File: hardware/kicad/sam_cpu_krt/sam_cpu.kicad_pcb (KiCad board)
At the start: 4 copper layers, 142 x 236.8 mm, 459 parts, among them J1 J1 SWITCH COLUMNS, J10 J10 SPEAKERS, J11 J11 POWER, J12 J12 SWITCH ROWS, J13 J13 DEDICATED, J17 EXT 5V, J18 J18 GI DIMMER, J19 USB-C (to Pi), J2 J2 DEDICATED, J20 SWD, J21 Raspberry Pi 40-pin, J22 J22 STEREO, J23 EXT 12V, J24 J24 SUBWOOFER, J27 J27 RS485 IN, J28 J28 I2S IN, J29 J29 RS485 OUT, J3 J3 DEDICATED, J30 J30 LINE IN, J6 J6 SWITCH ROWS, J9 J9 IO BUS, Q1 AO3401A, Q11 MMBT3904, Q12 MMBT3904, Q13 MMBT3904, Q14 MMBT3904, Q15 MMBT3904, Q16 MMBT3904, Q17 MMBT3904, Q18 MMBT3904, Q2 AO3401A, Q3 2N7002, Q4 2N7002, SW1 RESET, SW2 BOOTSEL, SW3 DIP x8, U1 LTC4412, U10 LM339, U11 LM339, U14 74HC165, U15 74HC165, U16 74HC165, U17 74HC165, U18 74HC165, U19 74HC165, U2 LTC4412, U20 74HC595, U22 PCM5102A, U23 TDA7297, U24 TDA7297, U25 DS3231MZ, U26 OPA1678, U3 NCP1117-3.3, U30 74HC165, U31 74HC595, U32 ADM2682E, U4 RP2354B, U5 TPS3808G33, U6 SN74LVC8T245, U7 74AHCT541, U8 LM339, U9 LM339, Y1 12MHz

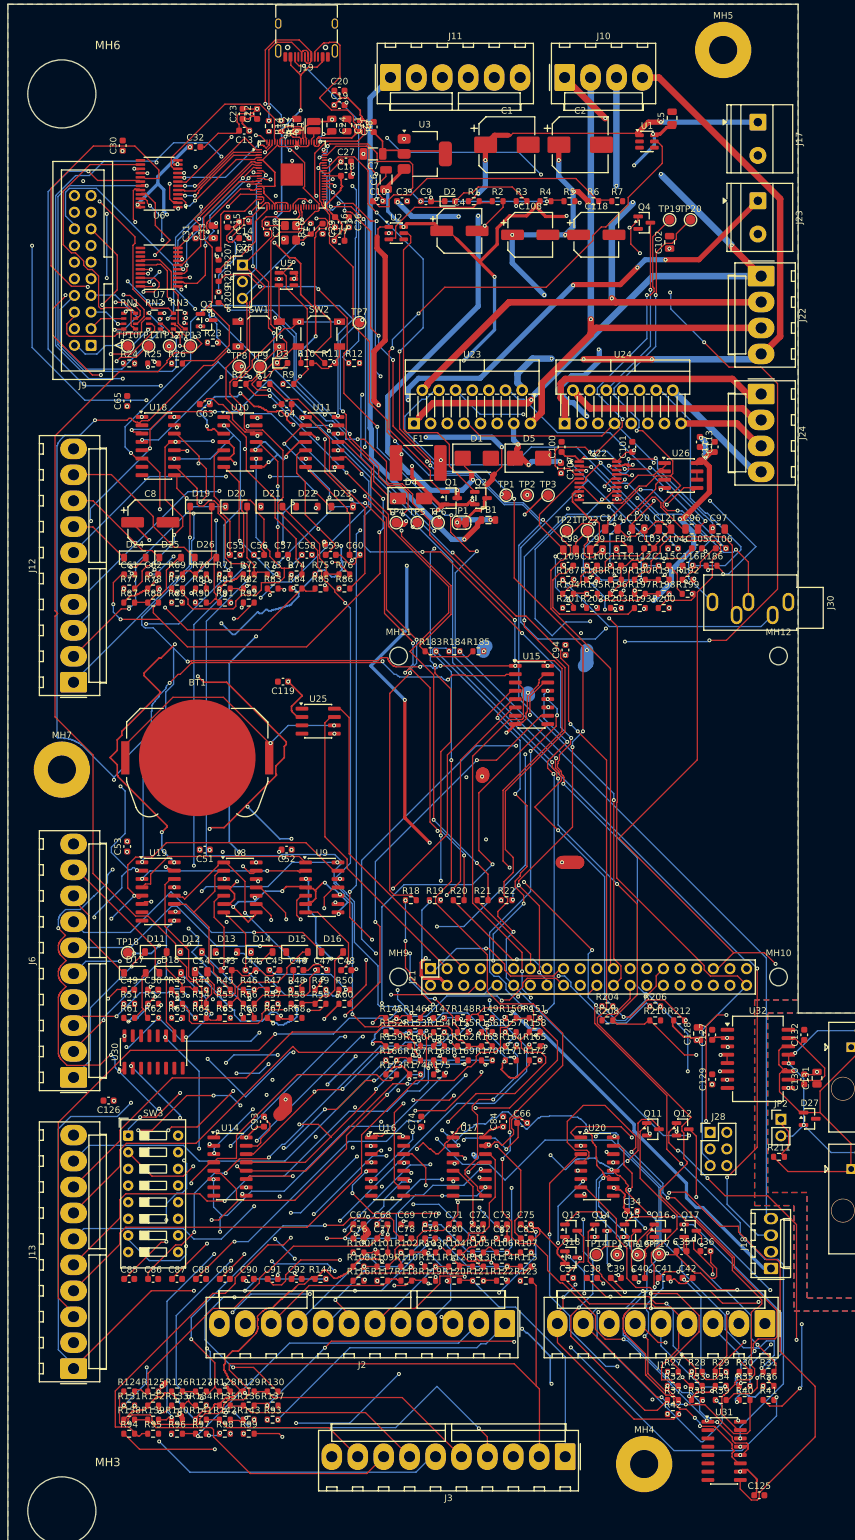
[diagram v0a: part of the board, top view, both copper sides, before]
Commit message: KRT board: check against the JLCPCB 4-layer rules and reroute the nets they flag
Adds the project's JLCPCB rules (sam_cpu.kicad_dru and board minimums) to the KRT
clone. 24 nets with different-net vias under 0.5 mm hole to hole, or a stub
0.25 mm from the MH11 hole, were rerouted; JLC hole errors are now 0.

Co-Authored-By: Claude Opus 5.5 (1M context) <noreply@anthropic.com>
Claude-Session: https://claude.ai/code/session_012mQXTyxPh1ZSDfsNXZEFhJ
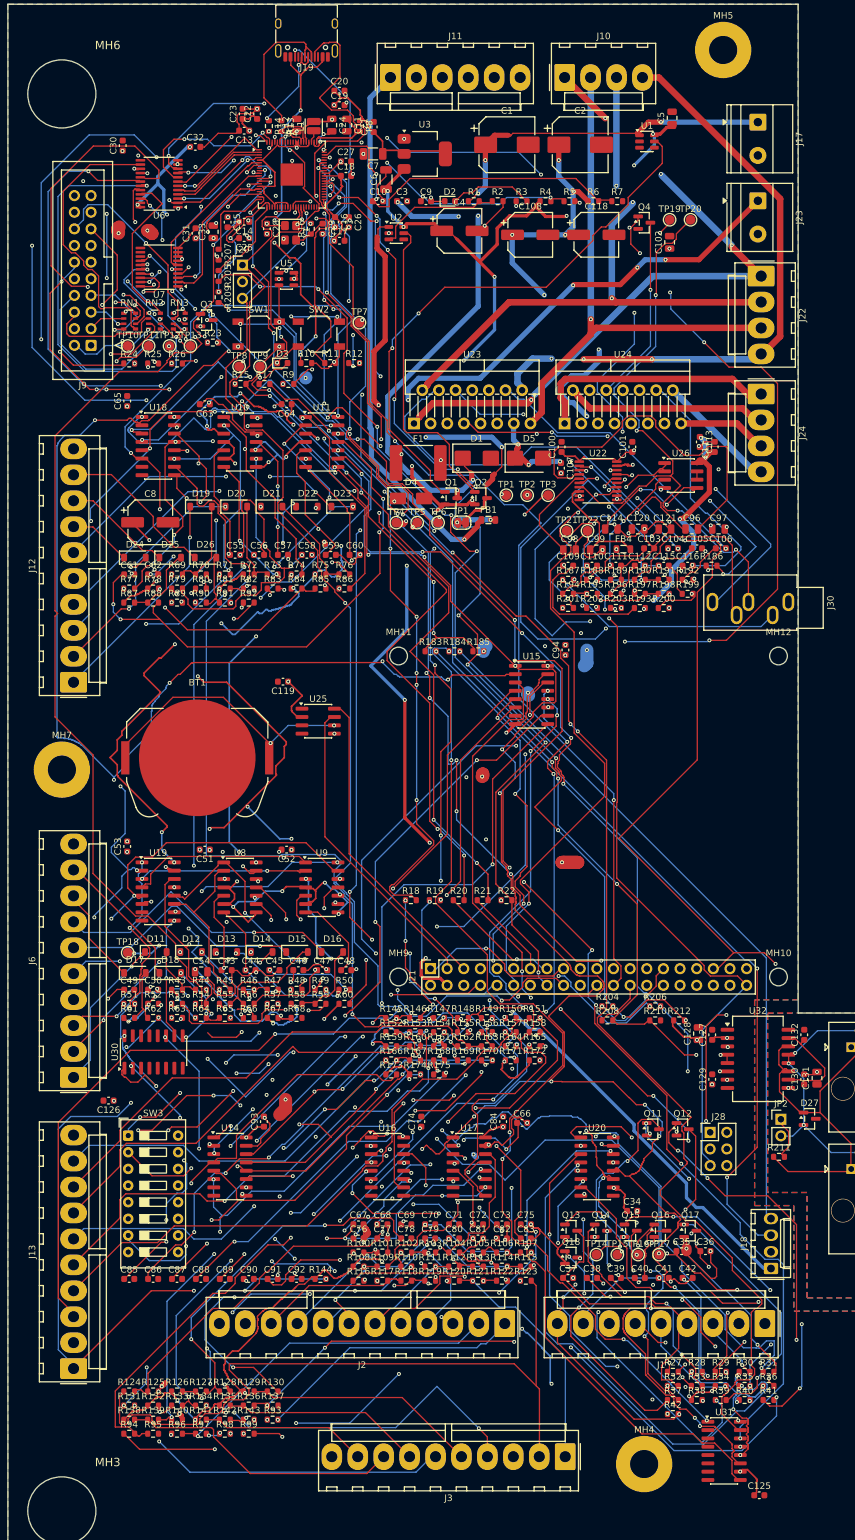
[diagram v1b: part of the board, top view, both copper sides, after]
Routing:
- net GND: track 400.7 -> 474.8 mm, vias 133 -> 148
- net SW_LOAD_N: track 347.5 -> 405.5 mm, vias 23 -> 24
- net BUS_A2: track 22.4 -> 1.27 mm, vias 2 -> 1
- net Net-(U22-CAPM): track 34.7 -> 54.3 mm, vias 4 -> 0
- net Net-(J1-Pin_8): track 63.0 -> 52.1 mm
- net Net-(J9-Pin_18): track 33.8 -> 23.6 mm
- net AUD_DAC_L: track 83.3 -> 91.6 mm, vias 4 -> 5
- net Net-(J9-Pin_12): track 40.1 -> 46.9 mm, vias 3 -> 5
- net Net-(Q11-B): track 49.4 -> 42.6 mm, vias 2 -> 3
- net BUS_D2: track 16.7 -> 23.5 mm
- net Net-(RN3-R2.2): track 11.2 -> 18.0 mm, vias 2 -> 3
- net Net-(J9-Pin_16): track 36.4 -> 29.6 mm
- net /MCU and Pi/MR_N: track 115.4 -> 121.7 mm, vias 10 -> 7
- net FRAME_SCK: track 155.8 -> 150.1 mm, vias 4 -> 9
- net NBRESET_DRV: track 42.6 -> 37.0 mm, vias 0 -> 4
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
